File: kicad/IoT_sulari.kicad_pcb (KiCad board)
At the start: 2 copper layers, 39 parts, among them J1 73412-0110, J2 73412-0110, J20 694106106102, J40 693043020611, SW2 TL3301DF160QG, SW3 TL3301DF160QG, SW4 TL3301DF160QG, SW5 TL3301DF160QG, U2 NRF9160-SICA-B1A-R, U20 MIC5219-3.3YM5-TR, U30 SHT40-AD1B-R2, U31 TMP117MAIDRVT, U40 TPD3F303DPVR

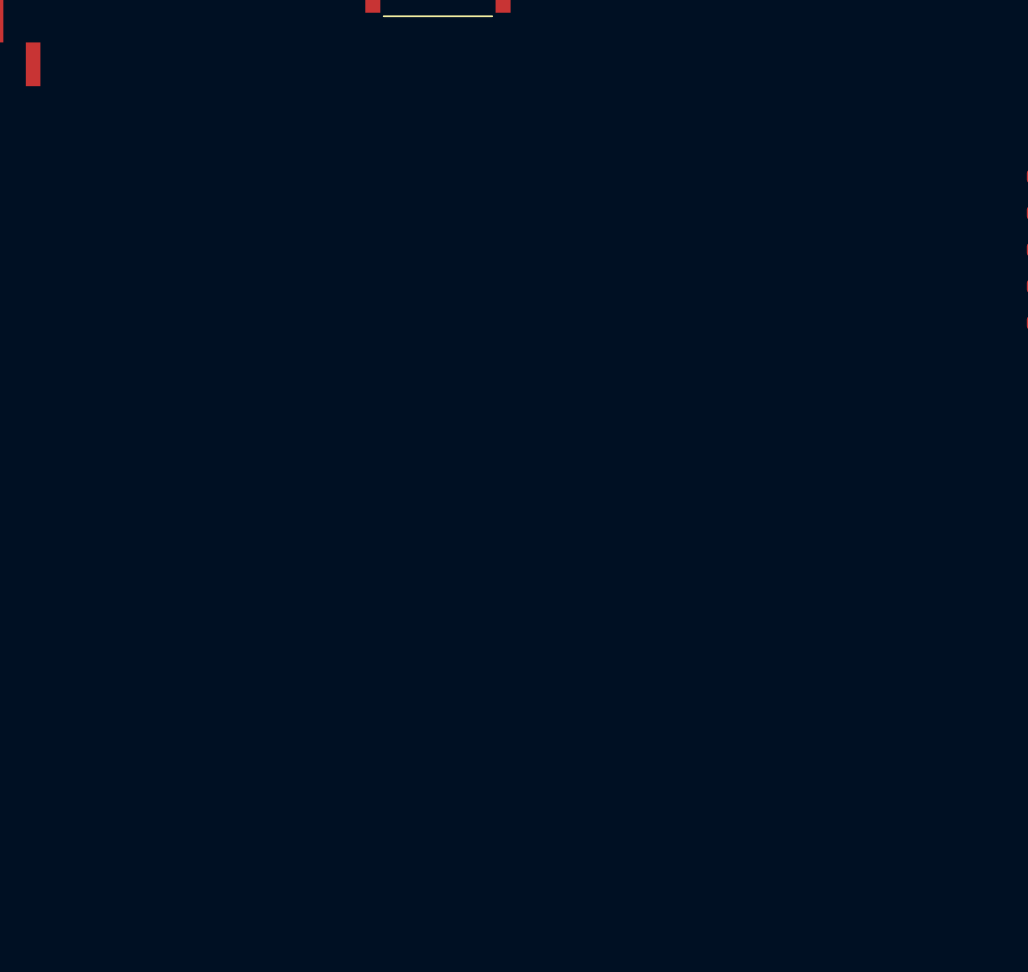
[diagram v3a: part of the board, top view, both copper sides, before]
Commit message: Reset button footprint added to pcb
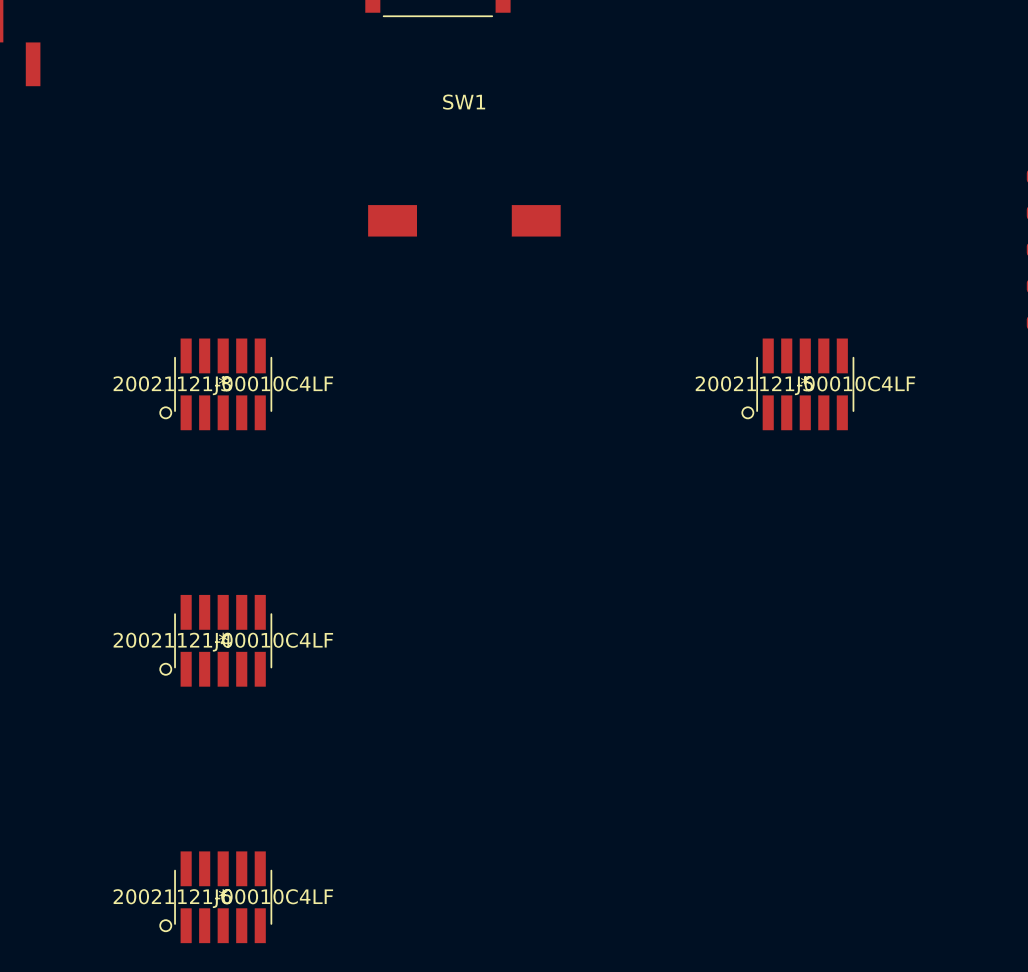
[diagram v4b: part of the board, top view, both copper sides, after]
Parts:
- added J3: 20021121-00010C4LF, 20021121-00010C4LF:20021121-00010C4LF, F.Cu at (140.4, 114.9)
- added J4: 20021121-00010C4LF, 20021121-00010C4LF:20021121-00010C4LF, F.Cu at (140.4, 132.5)
- added J5: 20021121-00010C4LF, 20021121-00010C4LF:20021121-00010C4LF, F.Cu at (180.3, 114.9)
- added J6: 20021121-00010C4LF, 20021121-00010C4LF:20021121-00010C4LF, F.Cu at (140.4, 150.0)
- added SW1: SW_SPST, TL3302BF180QG:TL3302BF180QG, F.Cu at (157.0, 103.7)

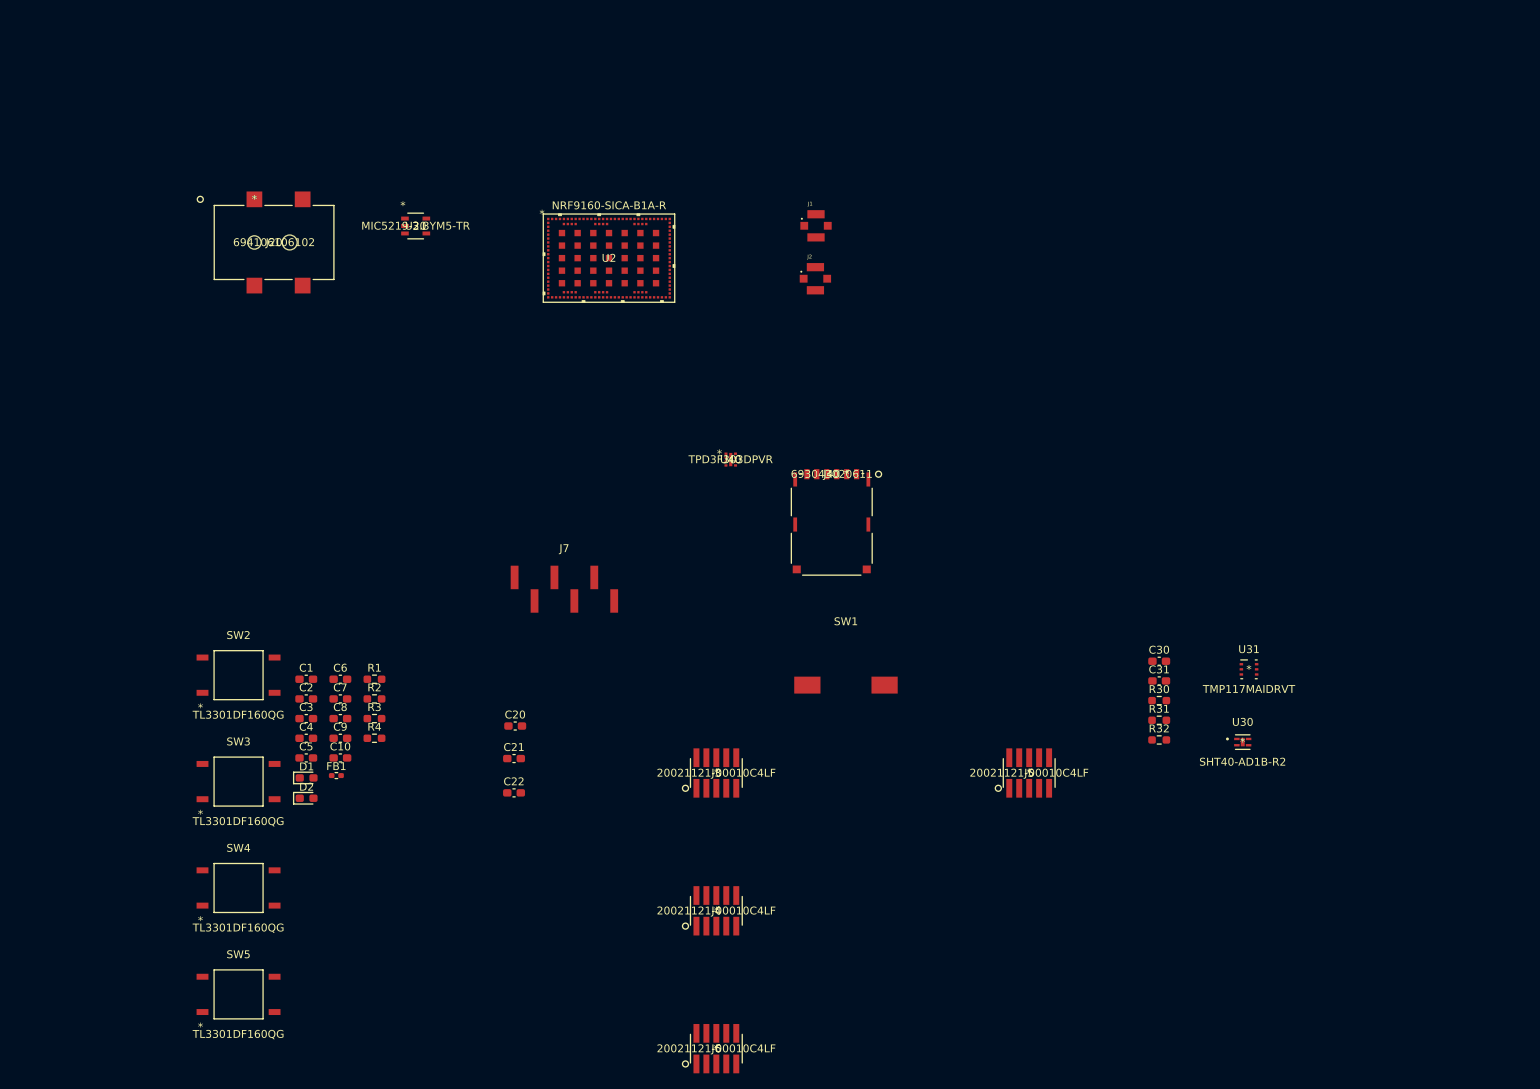
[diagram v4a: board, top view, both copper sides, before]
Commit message: Updated PCB design rules and layout to correct placing around nRF9160
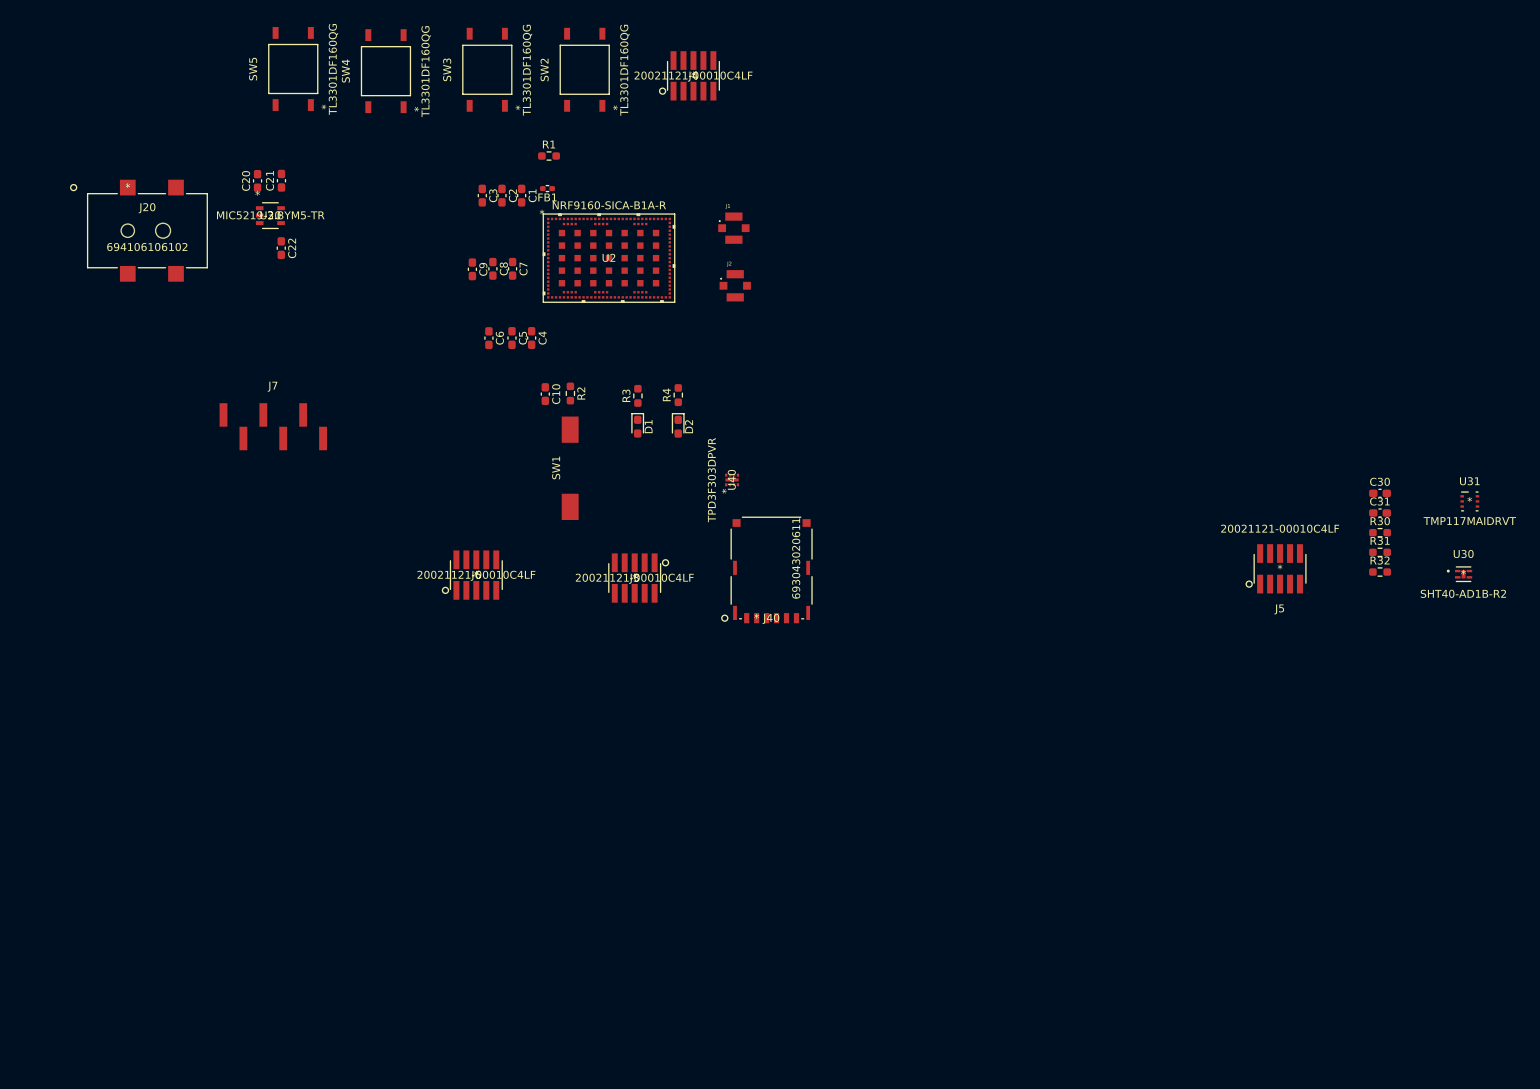
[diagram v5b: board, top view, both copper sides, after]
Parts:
- moved SW5 118.2 mm to (86.5, 25.1), turned to 90 degrees
- moved J4 106.5 mm to (137.5, 26.0)
- moved SW4 105.9 mm to (98.3, 25.4), turned to 90 degrees
- moved SW3 96.2 mm to (111.2, 25.2), turned to 90 degrees
- moved SW2 88.9 mm to (123.7, 25.2), turned to 90 degrees
- moved FB1 79.6 mm to (118.9, 40.4), turned to 180 degrees
- moved C21 79.4 mm to (85.0, 39.4), turned to 90 degrees
- moved C20 76.9 mm to (81.9, 39.4), turned to 90 degrees
- moved C22 75.6 mm to (85.0, 48.0), turned to -90 degrees
- moved C3 70.4 mm to (110.6, 41.2), turned to -90 degrees
- moved R1 70.3 mm to (119.1, 36.2)
- moved C2 68.9 mm to (113.1, 41.2), turned to -90 degrees
- moved J6 67.7 mm to (109.8, 89.6)
- moved C1 67.5 mm to (115.6, 41.2), turned to -90 degrees
- moved D2 67.0 mm to (135.6, 70.7), turned to -90 degrees
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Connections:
- net Net-(#PWR011-+3.3V) renamed /VDD1
- net Net-(#PWR012-+3.3V) renamed /VDD2
- net Net-(#PWR019-+3.3V) renamed /DISPLAY_PWR
- net Net-(#PWR025-+3.3V) renamed /VDD_GPIO
- net Net-(#PWR028-+3.3V) renamed /SENSORBOARD_PWR
- net Net-(#PWR04-GND) renamed /GND_SHIELD-GND
- net Net-(J1-SIG) renamed /GPS_ant
- net Net-(J2-SIG) renamed /ANT
- net VCC renamed UART_VCC
- J20 pad 4: (no net) -> Net-(U20-EN)
- U2 pad 100: BUTTON3 -> unconnected-(U2A-P0-04-Pad100)
- U2 pad 15: CLK -> UART_RTS
- U2 pad 16: CS -> UART_RXD
- U2 pad 18: DC -> UART_TXD
- U2 pad 19: RST -> UART_CTS
- U2 pad 2: BUTTON4 -> unconnected-(U2A-P0-05-Pad2)
- U2 pad 20: BUSY -> unconnected-(U2A-P0-12-Pad20)
- U2 pad 23: UART_RTS -> DIN
- U2 pad 24: UART_RXD -> CLK
- U2 pad 25: UART_TXD -> CS
- U2 pad 26: UART_CTS -> DC
- U2 pad 28: unconnected-(U2A-P0-17/AIN4-Pad28) -> RST
- U2 pad 29: unconnected-(U2A-P0-18/AIN5-Pad29) -> BUSY
- U2 pad 37: unconnected-(U2A-P0-21/TRACECLK-Pad37) -> STATUS_LED_RED
- U2 pad 38: unconnected-(U2A-P0-22/TRACEDATA0-Pad38) -> STATUS_LED_GREEN
- U2 pad 4: DIN -> unconnected-(U2A-P0-07-Pad4)
- U2 pad 95: STATUS_LED_RED -> BUTTON1
- U2 pad 96: STATUS_LED_GREEN -> BUTTON2
- U2 pad 97: BUTTON1 -> BUTTON3
- U2 pad 99: BUTTON2 -> BUTTON4
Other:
- copper layers 2 -> 4
- rule pad_to_mask_clearance: 0 -> 0.05

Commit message: updated PCB
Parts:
- D1, D2, R3, R4, SW2, SW3, SW4, SW5: moved to B.Cu
- U2: value NRF9160-SICA-B1A-R -> NRF9160
- moved J20 37.4 mm to (101.3, 50.5)
- moved D2 37.3 mm to (104.6, 49.9), turned to 180 degrees
- moved J40 36.4 mm to (138.0, 59.5), turned to 0 degrees
- moved D1 35.2 mm to (104.5, 47.0), turned to 180 degrees
- moved R4 32.0 mm to (108.4, 49.9), turned to 0 degrees
- moved R3 29.7 mm to (108.4, 47.0), turned to 0 degrees
- moved U20 25.7 mm to (109.2, 43.8)
- moved C21 24.8 mm to (109.7, 40.5), turned to 180 degrees
- moved C22 24.8 mm to (109.7, 47.2), turned to 180 degrees
- moved C20 22.9 mm to (104.6, 42.8), turned to 180 degrees
- moved U40 22.6 mm to (133.5, 56.8)
- moved J3 21.6 mm to (126.5, 68.8), turned to 0 degrees
- moved J6 21.4 mm to (114.5, 68.8)
- moved J7 19.2 mm to (103.0, 68.2)
- moved J4 15.8 mm to (127.5, 38.2)
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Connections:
- C1 pad 1: /VDD1 -> /+3.3V
- C2 pad 1: /VDD1 -> /+3.3V
- C3 pad 1: /VDD1 -> /+3.3V
- FB1 pad 1: Net-(U2A-VDD1) -> /VDD1
- FB1 pad 2: /VDD1 -> /+3.3V
- R1 pad 1: Net-(U2A-VDD1) -> /VDD1
- U2 pad 102: Net-(U2A-VDD1) -> /VDD1
- U2 pad 2: unconnected-(U2A-P0-05-Pad2) -> STATUS_LED_RED
- U2 pad 3: unconnected-(U2A-P0-06-Pad3) -> STATUS_LED_GREEN
- U2 pad 37: STATUS_LED_RED -> unconnected-(U2A-P0-21/TRACECLK-Pad37)
- U2 pad 38: STATUS_LED_GREEN -> unconnected-(U2A-P0-22/TRACEDATA0-Pad38)

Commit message: kytkimen siirto
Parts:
- moved SW1 3.66 mm to (120.8, 62.3)
- moved C10 0.25 mm to (126.2, 57.5)
- moved R2 0.25 mm to (123.5, 57.5)
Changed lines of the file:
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@@
   (net 127 "/+3.3V")
   (footprint "Resistor_SMD:R_0603_1608Metric_Pad0.98x0.95mm_HandSolder" (layer "F.Cu")
-    (at 123.5 57.749589 -90)
+    (at 123.5 57.5 -90)
     (descr "Resistor SMD 0603 (1608 Metric), square (rectangular) end terminal, IPC_7351 nominal with elongated pad for handsoldering. (Body size source: IPC-SM-782 page 72, https://www.pcb-3d.com/wordpress/wp-content/uploads/ipc-sm-782a_amendment_1_and_2.pdf), generated with kicad-footprint-generator")
     (tags "resistor handsolder")
@@
   )
   (footprint "Capacitor_SMD:C_0603_1608Metric_Pad1.08x0.95mm_HandSolder" (layer "F.Cu")
-    (at 126.25 57.75 -90)
+    (at 126.25 57.500411 -90)
     (descr "Capacitor SMD 0603 (1608 Metric), square (rectangular) end terminal, IPC_7351 nominal with elongated pad for handsoldering. (Body size source: IPC-SM-782 page 76, https://www.pcb-3d.com/wordpress/wp-content/uploads/ipc-sm-782a_amendment_1_and_2.pdf), generated with kicad-footprint-generator")
     (tags "capacitor handsolder")
@@
   )
   (footprint "TL3302BF180QG:TL3302BF180QG" (layer "F.Cu")
-    (at 120.75 66 90)
+    (at 120.75 62.345 90)
     (property "Sheetfile" "IoT_sulari.kicad_sch")
     (property "Sheetname" "")

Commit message: moro
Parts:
- added H1: MountingHole_Pad, MountingHole:MountingHole_3.2mm_M3_Pad_Via, F.Cu at (54.3, 68.0)
- added H2: MountingHole_Pad, MountingHole:MountingHole_3.2mm_M3_Pad_Via, F.Cu at (54.3, 78.2)
- added H3: MountingHole_Pad, MountingHole:MountingHole_3.2mm_M3_Pad_Via, F.Cu at (54.3, 88.3)
- added H4: MountingHole_Pad, MountingHole:MountingHole_3.2mm_M3_Pad_Via, F.Cu at (54.3, 98.5)
- moved C21 4.24 mm to (106.7, 37.5)
- moved C22 4.24 mm to (106.7, 44.2)
- moved U20 4.24 mm to (106.2, 40.8)
- moved C20 3.29 mm to (102.0, 40.8), turned to -90 degrees
- moved J20 2.85 mm to (100.6, 47.8)
- moved J1 2.06 mm to (139.5, 40.0)
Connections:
- C10 pad 1: Net-(U2A-NRESET) -> NRESET
- J3 pad 1: unconnected-(J3-Pad1) -> Net-(J3-Pad1)
- J3 pad 10: unconnected-(J3-Pad10) -> NRESET
- J3 pad 2: unconnected-(J3-Pad2) -> SWDIO
- J3 pad 3: unconnected-(J3-Pad3) -> GND
- J3 pad 4: SWDIO -> SWDCLK
- J3 pad 5: SWDCLK -> GND
- J3 pad 6: SWDCLK -> unconnected-(J3-Pad6)
- J3 pad 7: SWDIO -> unconnected-(J3-Pad7)
- R2 pad 1: Net-(U2A-NRESET) -> NRESET
- U2 pad 32: Net-(U2A-NRESET) -> NRESET
